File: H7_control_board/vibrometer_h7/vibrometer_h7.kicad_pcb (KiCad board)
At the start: 4 copper layers, 69.5 x 69.5 mm, 215 parts, among them J201 Conn_01x04_Socket, J202 Conn_02x06, J204 TC2030-NL, J301 USB_C_Receptacle_USB2.0_16P, J501 Conn_02x08_Odd_Even, J502 Conn_02x08_Odd_Even, J601 Conn_01x08_Socket, J701 Conn_01x08_Socket, J801 Conn_01x08_Socket, J901 PH-313D, Q201 BSS138, Q202 BSS138, Q203 BSS138, SW201 SW_Push, SW501 SW_Push, SW502 SW_Push, U201 STM32H723VGTx, U301 USBLC6-2SC6, U302 MT9700, U303 AMS1117-3V3, U901 RC4580, U902 TPA6111A2, Y201 24MHz

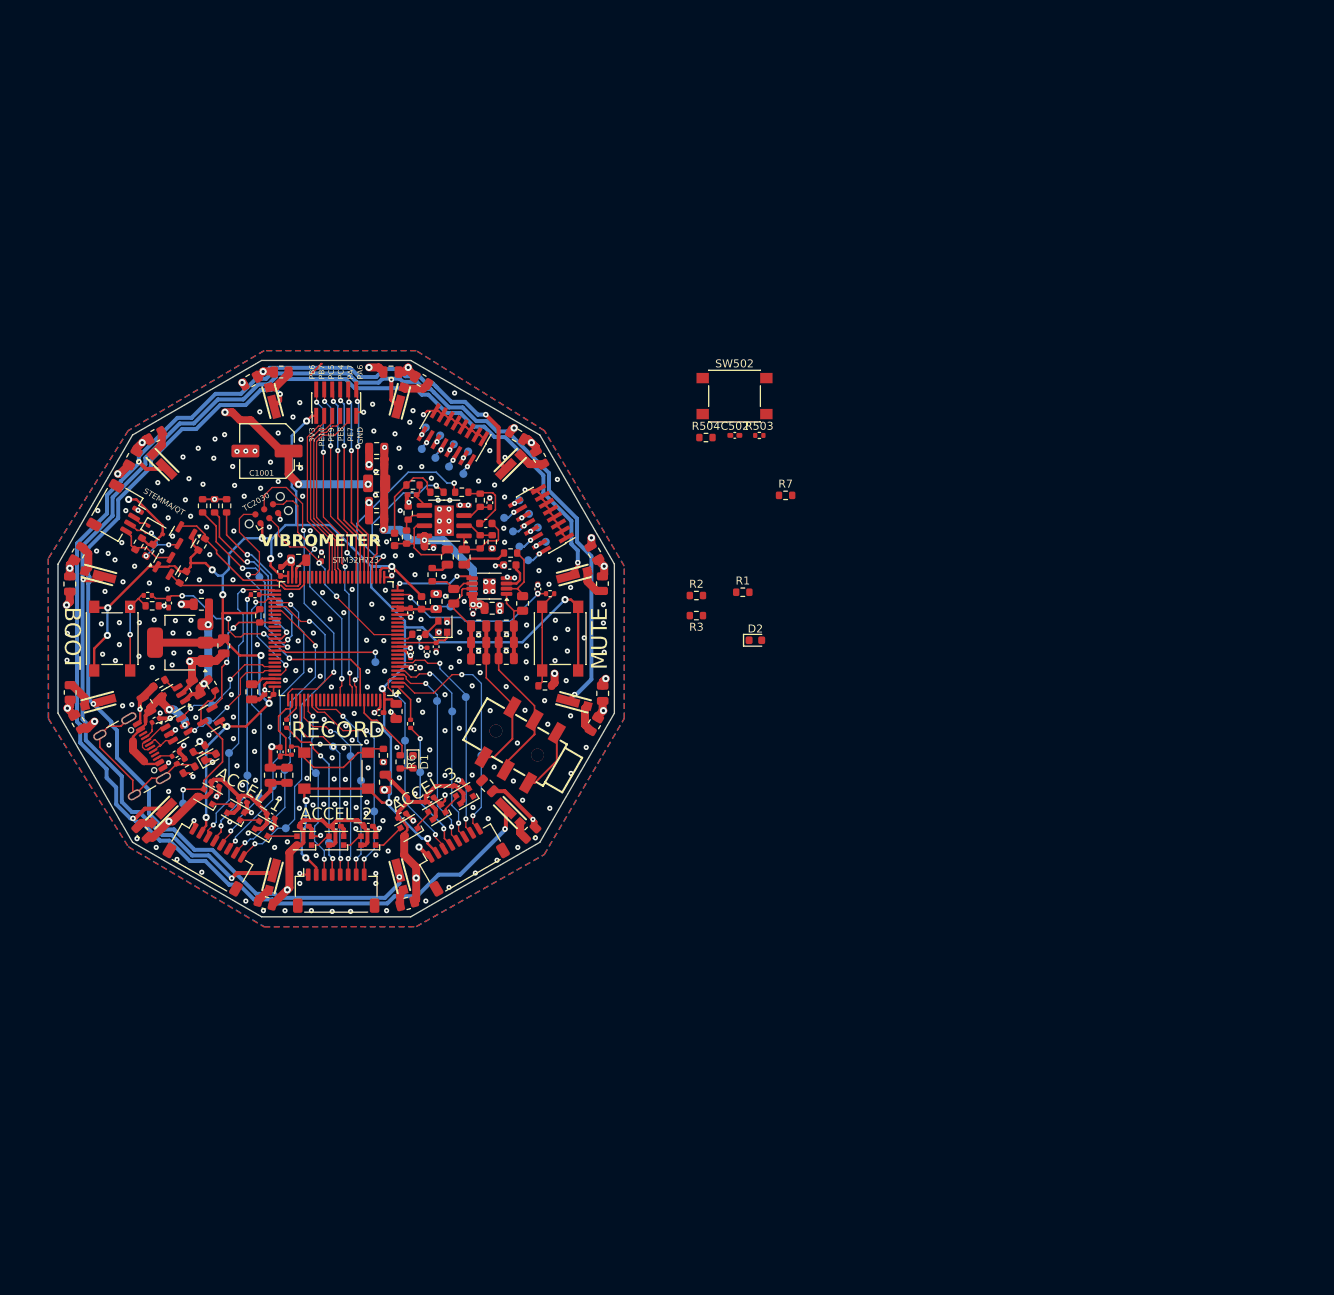
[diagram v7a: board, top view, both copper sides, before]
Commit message: connectors, they are so BIG whyyyy john, whyyy
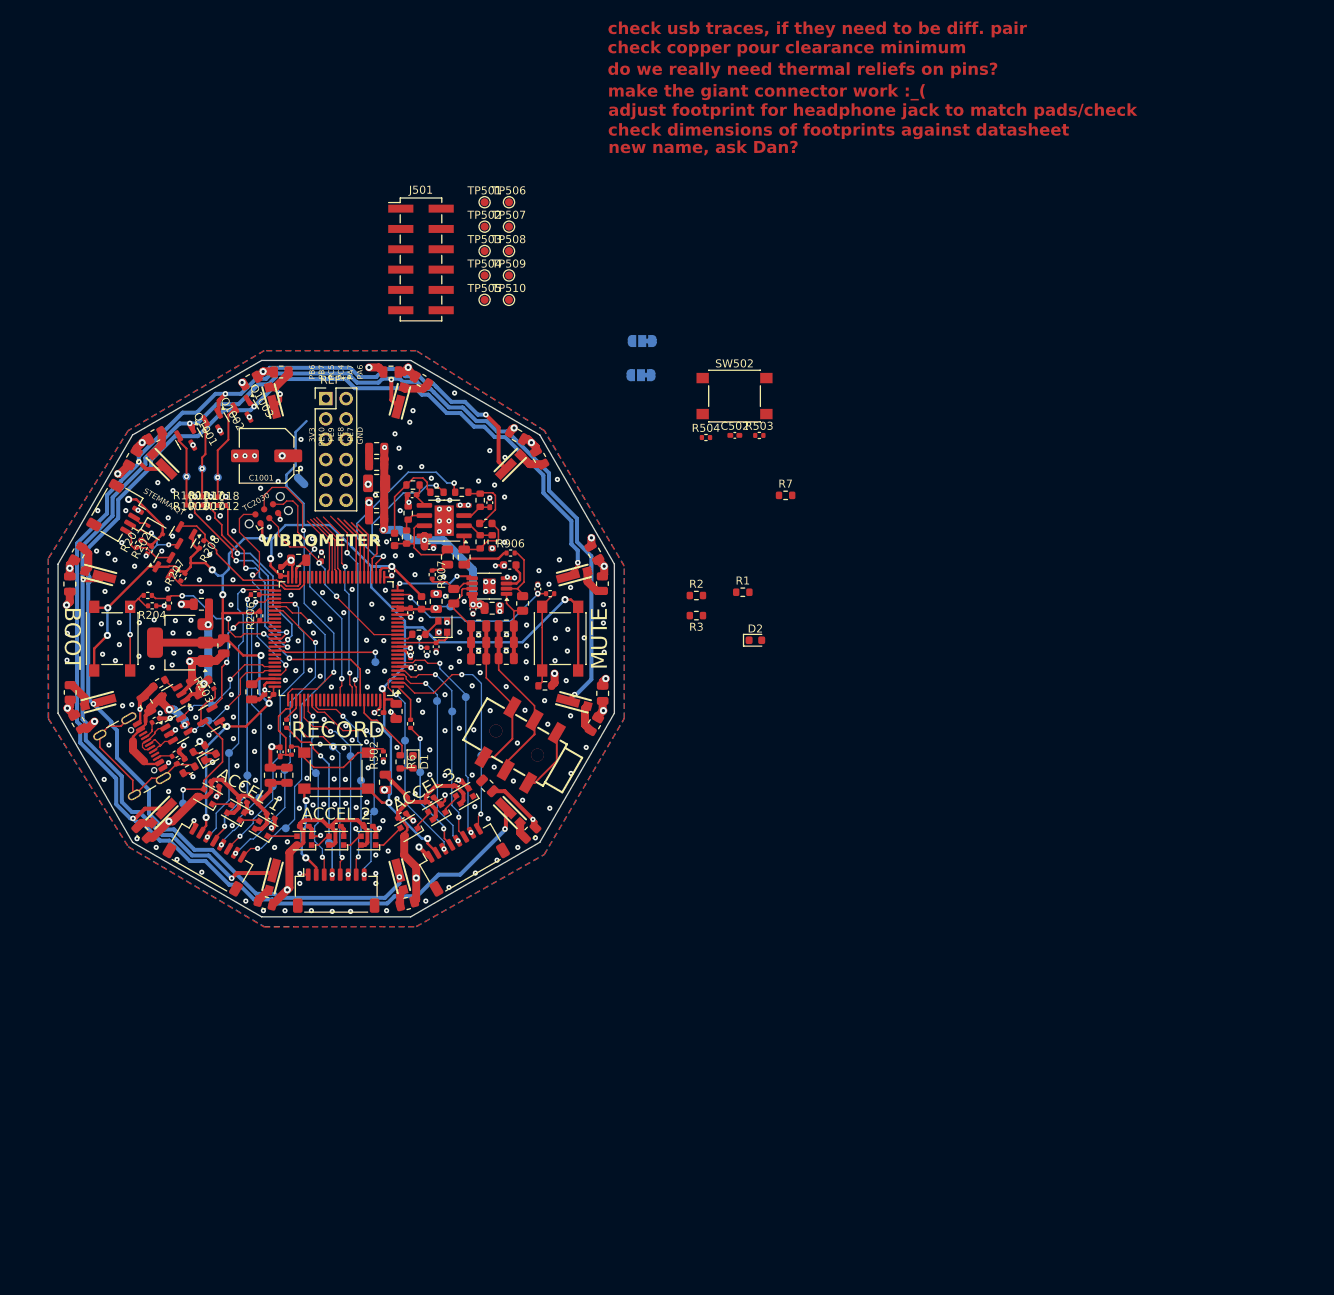
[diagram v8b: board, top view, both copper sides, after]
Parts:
- removed J202: Conn_02x06, Connector_PinHeader_1.00mm:PinHeader_2x06_P1.00mm_Vertical_SMD
- removed J502: Conn_02x08_Odd_Even, Connector_PinHeader_1.00mm:PinHeader_2x08_P1.00mm_Vertical_SMD
- removed TP511, TP512, TP513, TP514, TP515, TP516: TestPoint, TestPoint:TestPoint_Pad_D1.0mm
- added JP901: AMP2 FILT BYPASS, Jumper:SolderJumper-3_P1.3mm_Bridged12_RoundedPad1.0x1.5mm, B.Cu at (188.1, 67.1)
- added JP902: AMP1 FILT BYPASS, Jumper:SolderJumper-3_P1.3mm_Bridged12_RoundedPad1.0x1.5mm, B.Cu at (188.2, 62.8)
- added Q1001: NMOS, Package_TO_SOT_SMD:SOT-23, F.Cu at (131.6, 75.0)
- added Q1002: NMOS, Package_TO_SOT_SMD:SOT-23, F.Cu at (134.9, 73.1)
- added Q1003: NMOS, Package_TO_SOT_SMD:SOT-23, F.Cu at (138.6, 71.5)
- added R1001: 330, Resistor_SMD:R_0402_1005Metric, F.Cu at (131.8, 83.3)
- added R1017: 330, Resistor_SMD:R_0402_1005Metric, F.Cu at (133.8, 83.3)
- added R1018: 330, Resistor_SMD:R_0402_1005Metric, F.Cu at (135.7, 83.3)
- added REF**: PinHeader_2x06_P2.54mm_Vertical, Connector_PinHeader_2.54mm:PinHeader_2x06_P2.54mm_Vertical, F.Cu at (148.7, 70.0)
- C905, C916: value 100n -> C_Small
- J501: value Conn_02x08_Odd_Even -> debug_conn; footprint Connector_PinHeader_1.00mm:PinHeader_2x08_P1.00mm_Vertical_SMD -> Connector_PinHeader_2.54mm:PinHeader_2x06_P2.54mm_Vertical_SMD
- R1002, R1007, R1012, R201, R202, R203, R204, R206, R207, R208, R502, R504, R906, R907: footprint Resistor_SMD:R_0603_1608Metric -> Resistor_SMD:R_0402_1005Metric
- TP501, TP502, TP503, TP504, TP505, TP506, TP507, TP508, TP509, TP510: moved to F.Cu
- moved TP509 35.7 mm to (171.6, 54.6), turned to 0 degrees
- moved TP501 34.1 mm to (168.6, 45.5), turned to 0 degrees
- moved TP510 30.6 mm to (171.6, 57.6), turned to 0 degrees
- moved TP506 30.4 mm to (171.6, 45.5), turned to 0 degrees
- moved TP507 29.9 mm to (171.6, 48.5), turned to 0 degrees
- moved TP502 28.2 mm to (168.6, 48.5), turned to 0 degrees
- moved TP503 27.3 mm to (168.6, 51.5), turned to 0 degrees
- moved TP508 24.4 mm to (171.6, 51.5), turned to 0 degrees
- moved J501 22.5 mm to (160.6, 52.6), turned to 0 degrees
- moved TP504 21.4 mm to (168.6, 54.6), turned to 0 degrees
- moved TP1001 21.2 mm to (131.3, 79.8)
- moved TP505 20.7 mm to (168.6, 57.6), turned to 0 degrees
- moved TP1002 19.3 mm to (133.2, 78.8)
- moved TP1003 13.5 mm to (135.2, 79.8)
- moved R1002 3.20 mm to (131.8, 82.3), turned to 180 degrees
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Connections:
- C902 pad 1: /AUDIO/AMP1_OUT -> Net-(JP902-A)
- C912 pad 1: /AUDIO/AMP2_OUT -> Net-(JP901-A)
- J501 pad 11: GND -> Net-(J501-Pin_11)
- J501 pad 2: Net-(J501-Pin_2) -> GND
- J501 pad 3: GND -> Net-(J501-Pin_3)
- J501 pad 5: GND -> Net-(J501-Pin_5)
- J501 pad 7: GND -> Net-(J501-Pin_7)
- J501 pad 9: GND -> Net-(J501-Pin_9)
- R1002 pad 2: /MCU/LED_STROBE_1 -> Net-(Q1001-G)
- R1007 pad 2: /MCU/LED_STROBE_2 -> Net-(Q1002-G)
- R1012 pad 2: /MCU/LED_STROBE_3 -> Net-(Q1003-G)
- R904 pad 2: /AUDIO/AMP1_OUT -> Net-(JP902-A)
- R911 pad 2: /AUDIO/AMP2_OUT -> Net-(JP901-A)
- TP1001 pad 1: /MCU/LED_STROBE_1 -> Net-(Q1001-G)
- TP1002 pad 1: /MCU/LED_STROBE_2 -> Net-(Q1002-G)
- TP1003 pad 1: /MCU/LED_STROBE_3 -> Net-(Q1003-G)
- TP501 pad 1: Net-(J501-Pin_2) -> Net-(J501-Pin_11)
- TP502 pad 1: Net-(J501-Pin_4) -> Net-(J501-Pin_9)
- TP503 pad 1: Net-(J501-Pin_6) -> Net-(J501-Pin_7)
- TP504 pad 1: Net-(J501-Pin_8) -> Net-(J501-Pin_5)
- TP505 pad 1: Net-(J501-Pin_10) -> Net-(J501-Pin_3)
- TP507 pad 1: Net-(J501-Pin_14) -> Net-(J501-Pin_10)
- TP508 pad 1: Net-(J501-Pin_16) -> Net-(J501-Pin_8)
- TP509 pad 1: Net-(J502-Pin_2) -> Net-(J501-Pin_6)
- TP510 pad 1: Net-(J502-Pin_4) -> Net-(J501-Pin_4)
- U901 pad 1: /AUDIO/AMP1_OUT -> Net-(JP902-A)
- U901 pad 7: /AUDIO/AMP2_OUT -> Net-(JP901-A)
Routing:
- net GND: track 125.0 -> 102.6 mm, vias 325 -> 309
- net /MCU/ADC2_INP: track 24.2 -> 7.16 mm, vias 2 -> 0
- net /MCU/ADC2_INN: track 24.5 -> 7.49 mm, vias 2 -> 0
- net /MCU/ADC1_INP: track 24.5 -> 7.95 mm, vias 2 -> 0
- net /MCU/ADC1_INN: track 24.7 -> 8.31 mm, vias 2 -> 0
- net /MCU/VCP_TX: track 40.7 -> 24.4 mm, vias 4 -> 2
- net /MCU/VCP_RX: track 40.8 -> 24.7 mm, vias 4 -> 2
- net /MCU/UART_RX: track 23.9 -> 8.69 mm
- net /MCU/UART_TX: track 23.3 -> 8.48 mm
- net /MCU/UART_RTS: track 22.8 -> 8.34 mm
- net /MCU/UART_CTS: track 22.4 -> 8.23 mm
- net +5V: track 188.6 -> 176.3 mm, vias 18 -> 17
- net Net-(Q1003-G): track 0.00 -> 12.0 mm, vias 0 -> 1
- net Net-(Q1002-G): track 0.00 -> 9.72 mm, vias 0 -> 1
- net Net-(Q1001-G): track 0.00 -> 9.05 mm, vias 0 -> 1
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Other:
- board text added: "ACCEL 1"
- board text added: "ACCEL 2"
- board text added: "ACCEL 3"
- board text added: "adjust footprint for headphone jack to match pads/check"
- board text added: "check copper pour clearance minimum"
- board text added: "check dimensions of footprints against datasheet"
- board text added: "check usb traces, if they need to be diff. pair"
- board text added: "do we really need thermal reliefs on pins?"
- board text added: "make the giant connector work :_("
- board text added: "new name, ask Dan?"
- board text removed: "ACCEL_1"
- board text removed: "ACCEL_2"
- board text removed: "ACCEL_3"
- board text removed: "STM32H723"
